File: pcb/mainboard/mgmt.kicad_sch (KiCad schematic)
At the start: 102 parts, among them J10 FAN_01, J11 XILINX_JTAG, J12 JUMPER_0402_SPDT, J13 JUMPER_0402_SPDT, J14 RJ45, J15 PMOD_HOST, J48 CONN_01X10, J8 FAN_01, J9 CONN_01X03, U23 STM32H735-UFBGA176-25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

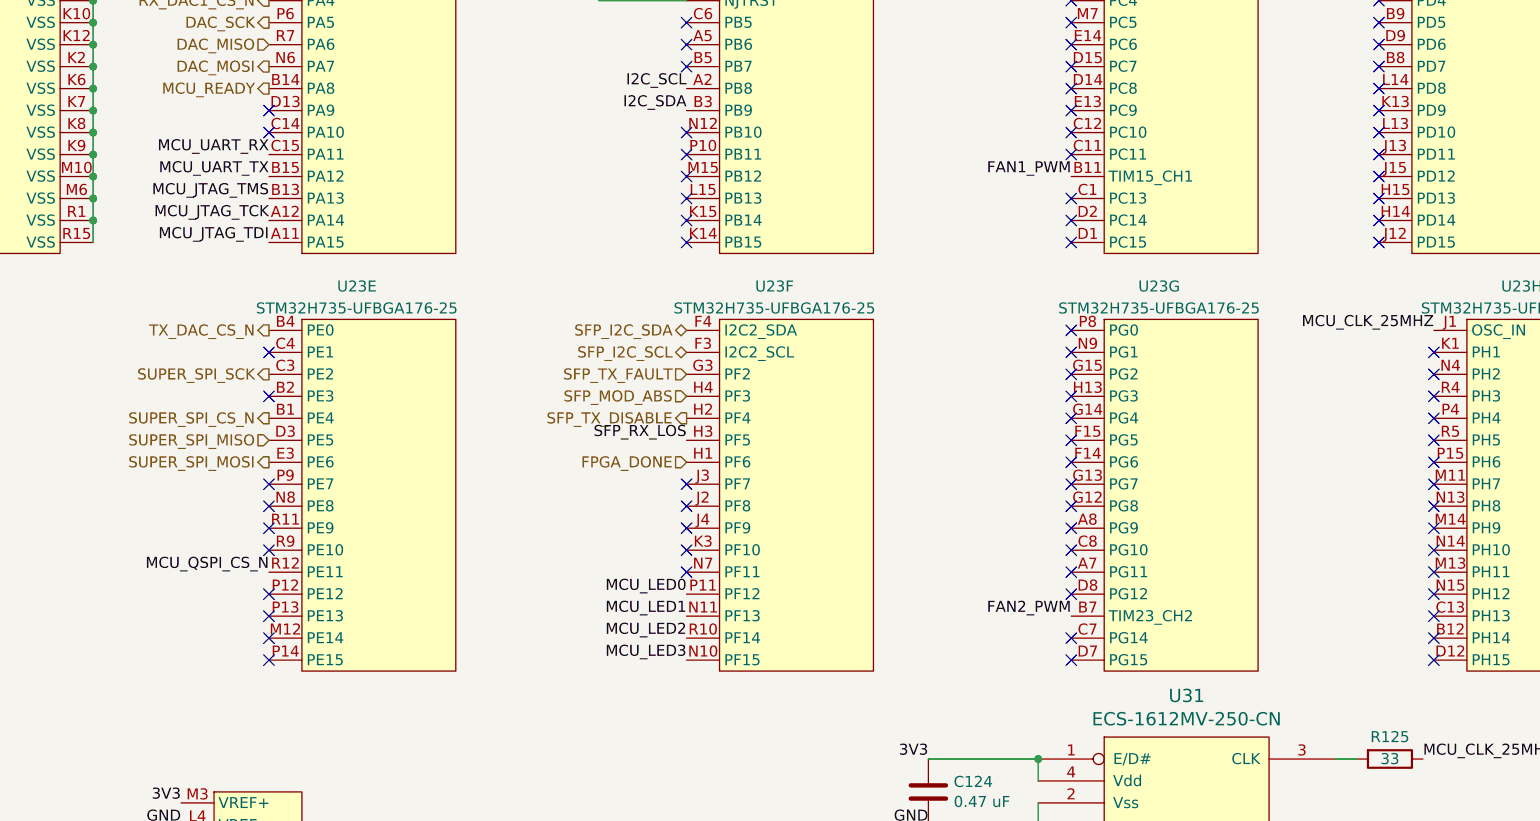
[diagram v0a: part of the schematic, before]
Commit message: Initial MCU subsystem layout
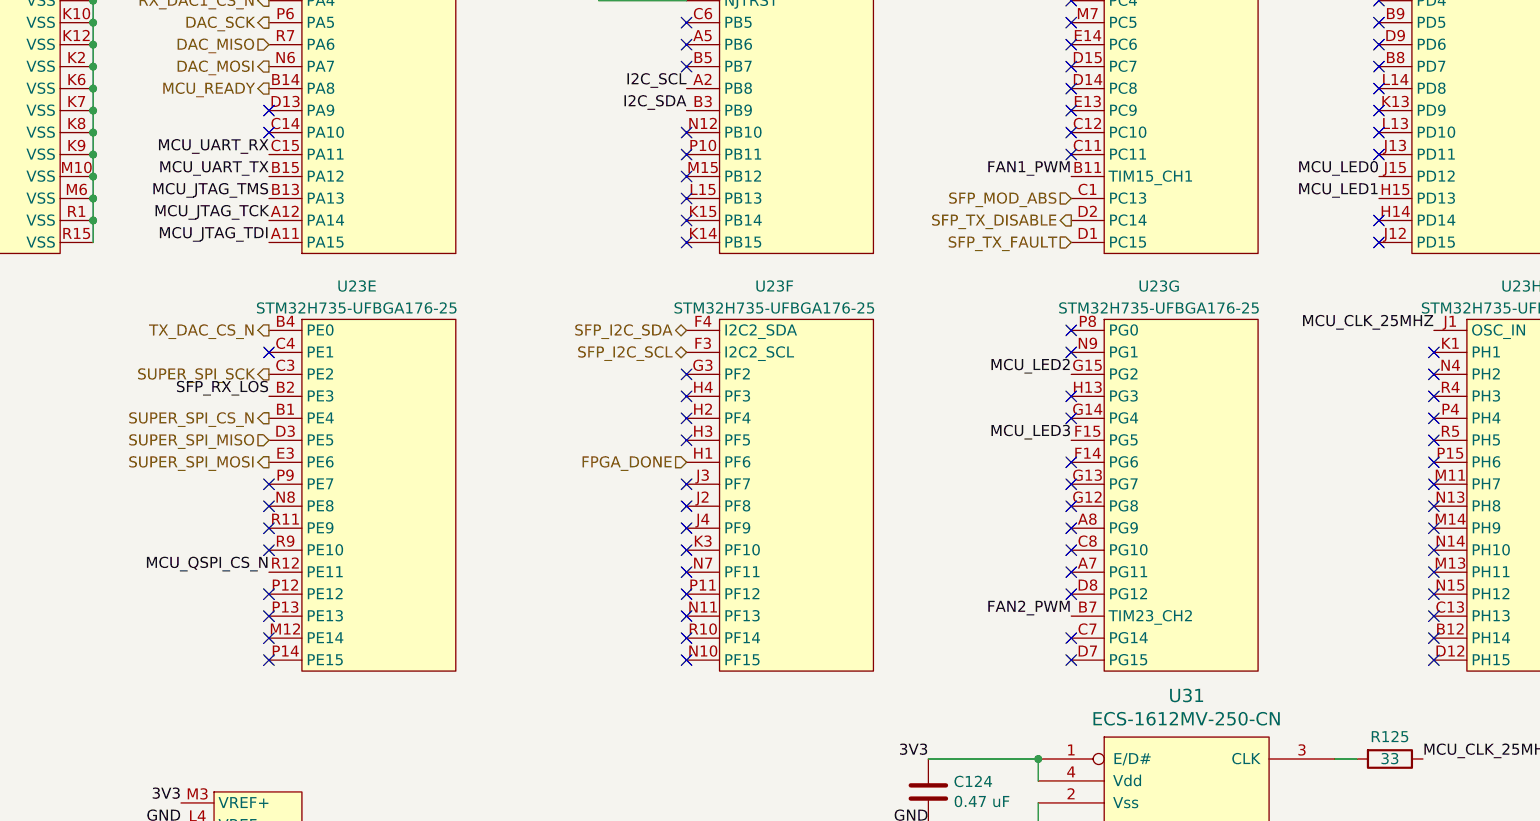
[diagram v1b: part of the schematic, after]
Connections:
- net MCU_LED0: now also U23.J15 (PD12); no longer U23.P11 (PF12)
- net MCU_LED1: now also U23.H15 (PD13); no longer U23.N11 (PF13)
- net MCU_LED2: now also U23.G15 (PG2); no longer U23.R10 (PF14)
- net MCU_LED3: now also U23.F15 (PG5); no longer U23.N10 (PF15)
- net SFP_MOD_ABS: now also U23.C1 (PC13); no longer U23.H4 (PF3)
- net SFP_RX_LOS: now also U23.B2 (PE3); no longer U23.H3 (PF5)
- net SFP_TX_DISABLE: now also U23.D2 (PC14); no longer U23.H2 (PF4)
- net SFP_TX_FAULT: now also U23.D1 (PC15); no longer U23.G3 (PF2)
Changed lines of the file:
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@@
   (junction (at 132.08 53.34) (diameter 0) (color 0 0 0 0)
   )
-  (no_connect (at 152.4 88.9))
   (no_connect (at 354.33 86.36))
   (no_connect (at 152.4 116.84))
@@
   (no_connect (at 287.02 93.98))
   (no_connect (at 152.4 83.82))
-  (no_connect (at 245.11 71.12))
   (no_connect (at 245.11 106.68))
   (no_connect (at 287.02 109.22))
@@
   (no_connect (at 245.11 104.14))
   (no_connect (at 280.67 58.42))
-  (no_connect (at 245.11 86.36))
   (no_connect (at 287.02 83.82))
   (no_connect (at 200.66 99.06))
   (no_connect (at 218.44 198.12))
   (no_connect (at 245.11 88.9))
-  (no_connect (at 245.11 93.98))
   (no_connect (at 354.33 73.66))
   (no_connect (at 280.67 48.26))
@@
   (no_connect (at 287.02 91.44))
   (no_connect (at 280.67 71.12))
+  (no_connect (at 200.66 119.38))
+  (no_connect (at 200.66 91.44))
   (no_connect (at 218.44 215.9))
   (no_connect (at 245.11 38.1))
@@
   (no_connect (at 354.33 63.5))
   (no_connect (at 354.33 101.6))
-  (no_connect (at 280.67 66.04))
   (no_connect (at 245.11 111.76))
   (no_connect (at 280.67 43.18))
@@
   (no_connect (at 200.66 60.96))
   (no_connect (at 280.67 60.96))
-  (no_connect (at 245.11 68.58))
   (no_connect (at 200.66 63.5))
   (no_connect (at 245.11 27.94))
@@
   (no_connect (at 287.02 104.14))
   (no_connect (at 354.33 83.82))
+  (no_connect (at 200.66 88.9))
   (no_connect (at 152.4 101.6))
   (no_connect (at 287.02 86.36))
@@
   (no_connect (at 245.11 81.28))
   (no_connect (at 354.33 91.44))
+  (no_connect (at 200.66 116.84))
+  (no_connect (at 200.66 111.76))
   (no_connect (at 280.67 50.8))
   (no_connect (at 152.4 55.88))
   (no_connect (at 245.11 55.88))
+  (no_connect (at 200.66 93.98))
   (no_connect (at 245.11 35.56))
   (no_connect (at 354.33 93.98))
   (no_connect (at 93.98 154.94))
   (no_connect (at 200.66 109.22))
+  (no_connect (at 200.66 86.36))
   (no_connect (at 354.33 48.26))
-  (no_connect (at 280.67 63.5))
   (no_connect (at 200.66 58.42))
   (no_connect (at 152.4 58.42))
@@
   (no_connect (at 354.33 106.68))
   (no_connect (at 152.4 119.38))
+  (no_connect (at 200.66 114.3))
   (no_connect (at 200.66 45.72))
   (no_connect (at 354.33 33.02))
@@
   (no_connect (at 354.33 50.8))
   (no_connect (at 245.11 96.52))
-  (no_connect (at 245.11 66.04))
   (no_connect (at 245.11 50.8))
   (no_connect (at 152.4 114.3))
@@
     (effects (font (size 1.27 1.27)) (justify right bottom))
   )
-  (label "MCU_LED3" (at 200.66 119.38 180)
+  (label "MCU_LED3" (at 245.11 93.98 180)
     (effects (font (size 1.27 1.27)) (justify right bottom))
   )
@@
     (effects (font (size 1.27 1.27)) (justify right bottom))
   )
-  (label "MCU_LED2" (at 200.66 116.84 180)
+  (label "MCU_LED2" (at 245.11 86.36 180)
     (effects (font (size 1.27 1.27)) (justify right bottom))
   )
@@
     (effects (font (size 1.27 1.27)) (justify right bottom))
   )
-  (label "MCU_LED1" (at 200.66 114.3 180)
+  (label "MCU_LED1" (at 280.67 66.04 180)
     (effects (font (size 1.27 1.27)) (justify right bottom))
   )
@@
     (effects (font (size 1.27 1.27)) (justify left bottom))
   )
-  (label "SFP_RX_LOS" (at 200.66 93.98 180)
+  (label "SFP_RX_LOS" (at 152.4 88.9 180)
     (effects (font (size 1.27 1.27)) (justify right bottom))
   )
@@
     (effects (font (size 1.27 1.27)) (justify right bottom))
   )
-  (label "MCU_LED0" (at 200.66 111.76 180)
+  (label "MCU_LED0" (at 280.67 63.5 180)
     (effects (font (size 1.27 1.27)) (justify right bottom))
   )
@@
     (effects (font (size 1.27 1.27)) (justify right))
   )
-  (hierarchical_label "SFP_TX_DISABLE" (shape output) (at 200.66 91.44 180)
+  (hierarchical_label "SFP_TX_DISABLE" (shape output) (at 245.11 68.58 180)
     (effects (font (size 1.27 1.27)) (justify right))
   )
@@
     (effects (font (size 1.27 1.27)) (justify right))
   )
-  (hierarchical_label "SFP_TX_FAULT" (shape input) (at 200.66 86.36 180)
-    (effects (font (size 1.27 1.27)) (justify right))
-  )
-  (hierarchical_label "SFP_MOD_ABS" (shape input) (at 200.66 88.9 180)
-    (effects (font (size 1.27 1.27)) (justify right))
-  )
+  (hierarchical_label "SFP_TX_FAULT" (shape input) (at 245.11 71.12 180)
+    (effects (font (size 1.27 1.27)) (justify right))
+  )
+  (hierarchical_label "SFP_MOD_ABS" (shape input) (at 245.11 66.04 180)
+    (effects (font (size 1.27 1.27)) (justify right))
+  )

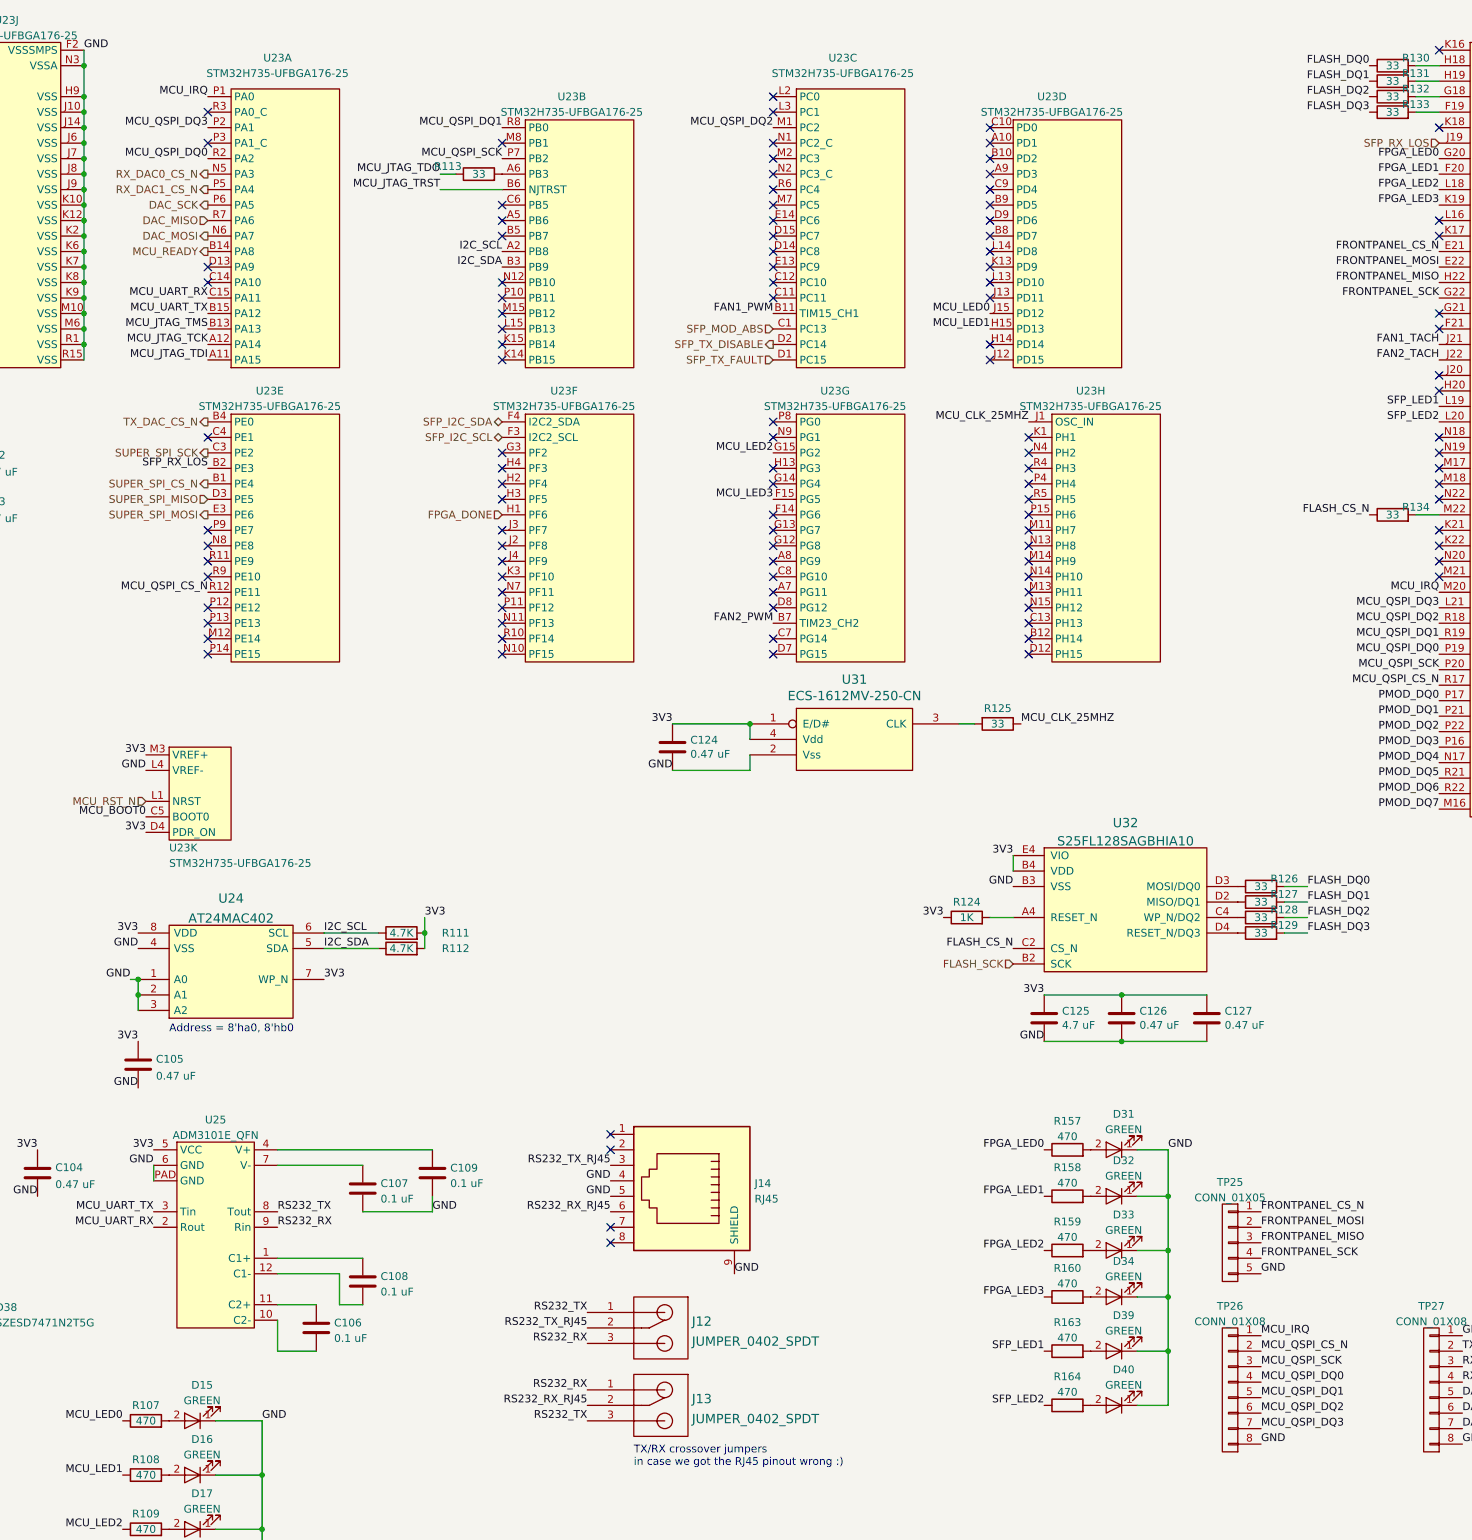
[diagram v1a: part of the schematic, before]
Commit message: Initial placement of rear I/O connectors
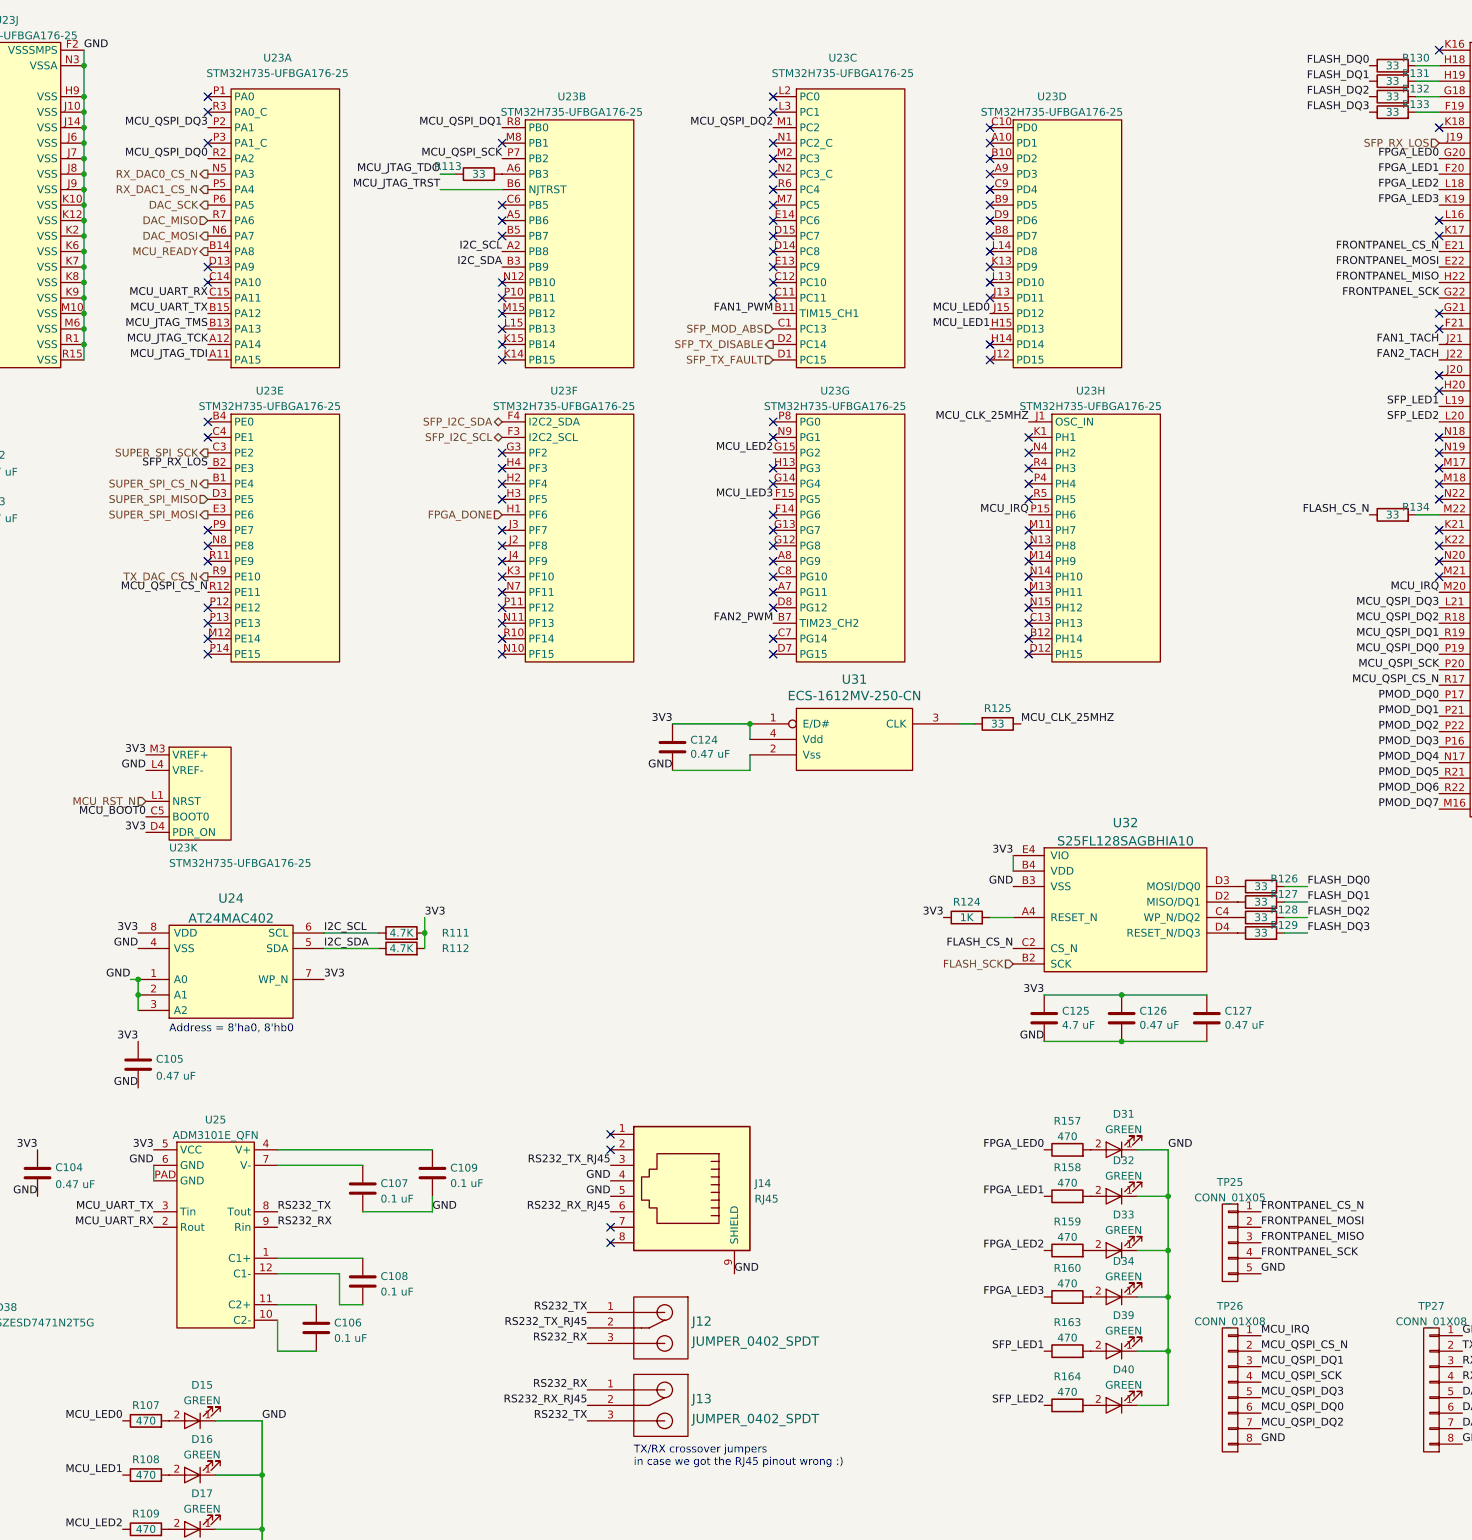
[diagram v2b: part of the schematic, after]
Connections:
- net MCU_IRQ: now also U23.P15 (PH6); no longer U23.P1 (PA0)
- net MCU_QSPI_DQ0: now also TP26.6 (P6); no longer TP26.4 (P4)
- net MCU_QSPI_DQ1: now also TP26.3 (P3); no longer TP26.5 (P5)
- net MCU_QSPI_DQ2: now also TP26.7 (P7); no longer TP26.6 (P6)
- net MCU_QSPI_DQ3: now also TP26.5 (P5); no longer TP26.7 (P7)
- net MCU_QSPI_SCK: now also TP26.4 (P4); no longer TP26.3 (P3)
- net TX_DAC_CS_N: now also U23.R9 (PE10); no longer U23.B4 (PE0)
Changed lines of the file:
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@@
   (no_connect (at 280.67 40.64))
   (no_connect (at 245.11 116.84))
+  (no_connect (at 152.4 27.94))
   (no_connect (at 354.33 63.5))
   (no_connect (at 354.33 101.6))
@@
   (no_connect (at 200.66 66.04))
   (no_connect (at 287.02 119.38))
-  (no_connect (at 152.4 106.68))
   (no_connect (at 200.66 60.96))
   (no_connect (at 280.67 60.96))
@@
   (no_connect (at 287.02 101.6))
   (no_connect (at 245.11 91.44))
+  (no_connect (at 152.4 81.28))
   (no_connect (at 152.4 35.56))
-  (no_connect (at 287.02 96.52))
   (no_connect (at 200.66 48.26))
   (no_connect (at 354.33 106.68))
@@
     (effects (font (size 1.27 1.27)) (justify right bottom))
   )
-  (label "MCU_QSPI_DQ1" (at 325.12 241.3 0)
+  (label "MCU_QSPI_DQ1" (at 325.12 236.22 0)
     (effects (font (size 1.27 1.27)) (justify left bottom))
   )
@@
     (effects (font (size 1.27 1.27)) (justify right bottom))
   )
-  (label "MCU_QSPI_DQ2" (at 325.12 243.84 0)
+  (label "MCU_QSPI_DQ2" (at 325.12 246.38 0)
     (effects (font (size 1.27 1.27)) (justify left bottom))
   )
@@
     (effects (font (size 1.27 1.27)) (justify right bottom))
   )
-  (label "MCU_QSPI_SCK" (at 325.12 236.22 0)
+  (label "MCU_QSPI_SCK" (at 325.12 238.76 0)
     (effects (font (size 1.27 1.27)) (justify left bottom))
   )
@@
     (effects (font (size 1.27 1.27)) (justify left bottom))
   )
-  (label "MCU_QSPI_DQ3" (at 325.12 246.38 0)
+  (label "MCU_QSPI_DQ3" (at 325.12 241.3 0)
     (effects (font (size 1.27 1.27)) (justify left bottom))
   )
@@
     (effects (font (size 1.27 1.27)) (justify right bottom))
   )
-  (label "MCU_QSPI_DQ0" (at 325.12 238.76 0)
+  (label "MCU_QSPI_DQ0" (at 325.12 243.84 0)
     (effects (font (size 1.27 1.27)) (justify left bottom))
   )
@@
     (effects (font (size 1.27 1.27)) (justify right bottom))
   )
-  (label "MCU_IRQ" (at 152.4 27.94 180)
+  (label "MCU_IRQ" (at 287.02 96.52 180)
     (effects (font (size 1.27 1.27)) (justify right bottom))
   )
@@
     (effects (font (size 1.27 1.27)) (justify right))
   )
-  (hierarchical_label "TX_DAC_CS_N" (shape output) (at 152.4 81.28 180)
+  (hierarchical_label "TX_DAC_CS_N" (shape output) (at 152.4 106.68 180)
     (effects (font (size 1.27 1.27)) (justify right))
   )
